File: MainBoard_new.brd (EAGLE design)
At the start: 60 parts, among them T1 BC847, U1 STM32F10XRXT6, Y1 8MHz, Y2 32.768kHz

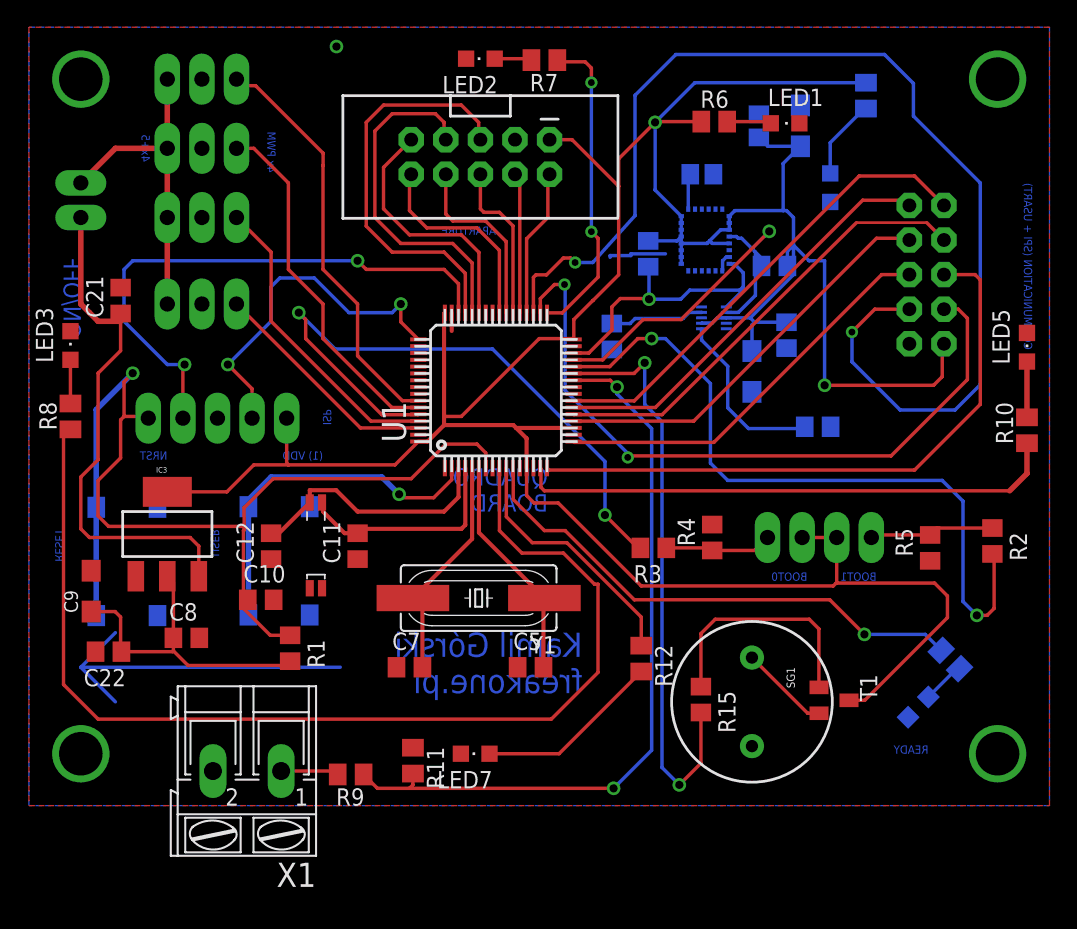
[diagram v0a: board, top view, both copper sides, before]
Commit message: zgubione sygnały przerwań
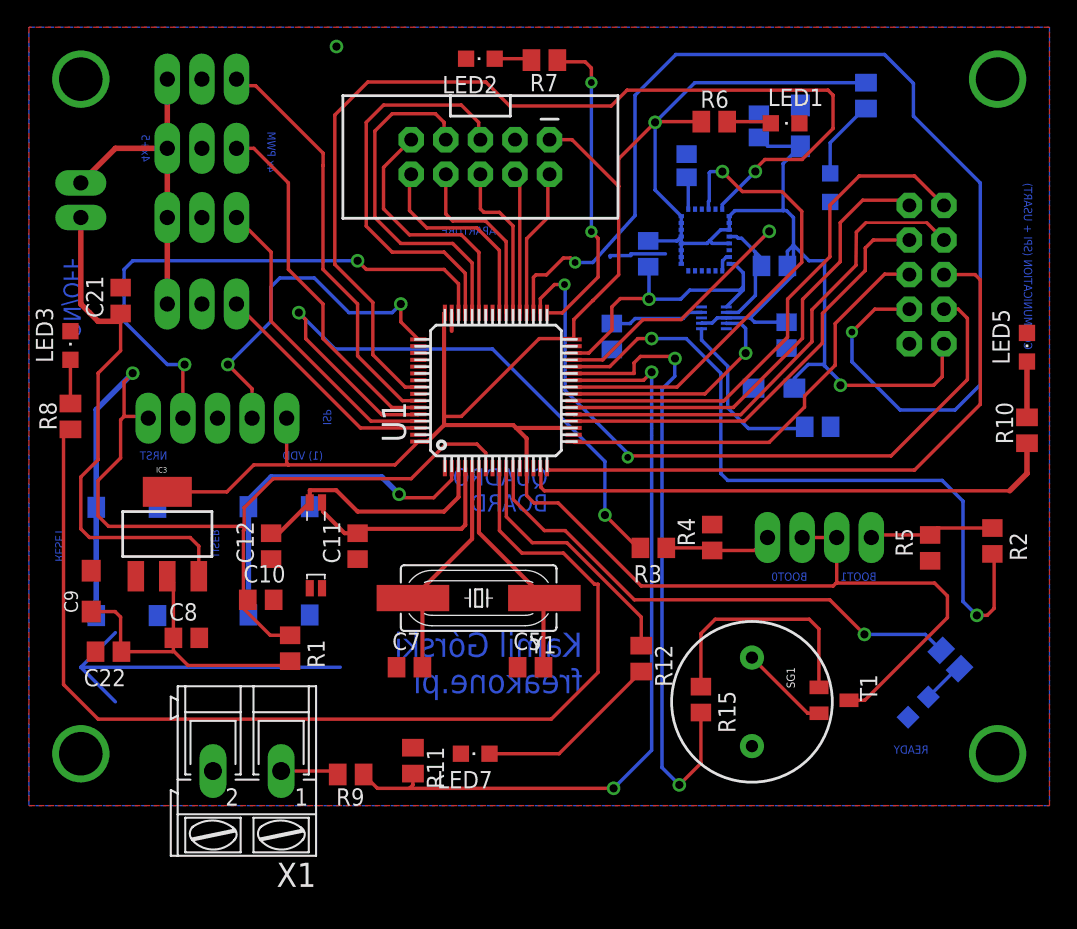
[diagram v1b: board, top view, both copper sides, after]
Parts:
- moved C17 2.03 mm to (44.5, 33.2), turned to 0 degrees
- moved C19 1.28 mm to (38.1, 49.5), turned to 90 degrees
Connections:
- net INT_ACC: now also U1.56
- net INT_GYRO: now also U1.25
- net INT_MAG: now also U1.24
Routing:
- net INT_ACC: track 0.00 -> 75.4 mm, vias 0 -> 1
- net INT_GYRO: track 0.00 -> 35.0 mm, vias 0 -> 1
- net INT_MAG: track 0.00 -> 17.3 mm, vias 0 -> 1
- net MOSI: track 34.9 -> 38.8 mm
- net MISO: track 31.1 -> 34.5 mm
- net BUZZ: track 43.6 -> 46.7 mm
- net SCK: track 33.5 -> 36.4 mm
- net LIPO: track 55.0 -> 57.7 mm
- net RX: track 29.8 -> 32.1 mm
- net SS: track 30.3 -> 32.4 mm
- net BOOT1: track 52.1 -> 53.0 mm
- net 3.3V: track 257.6 -> 258.1 mm

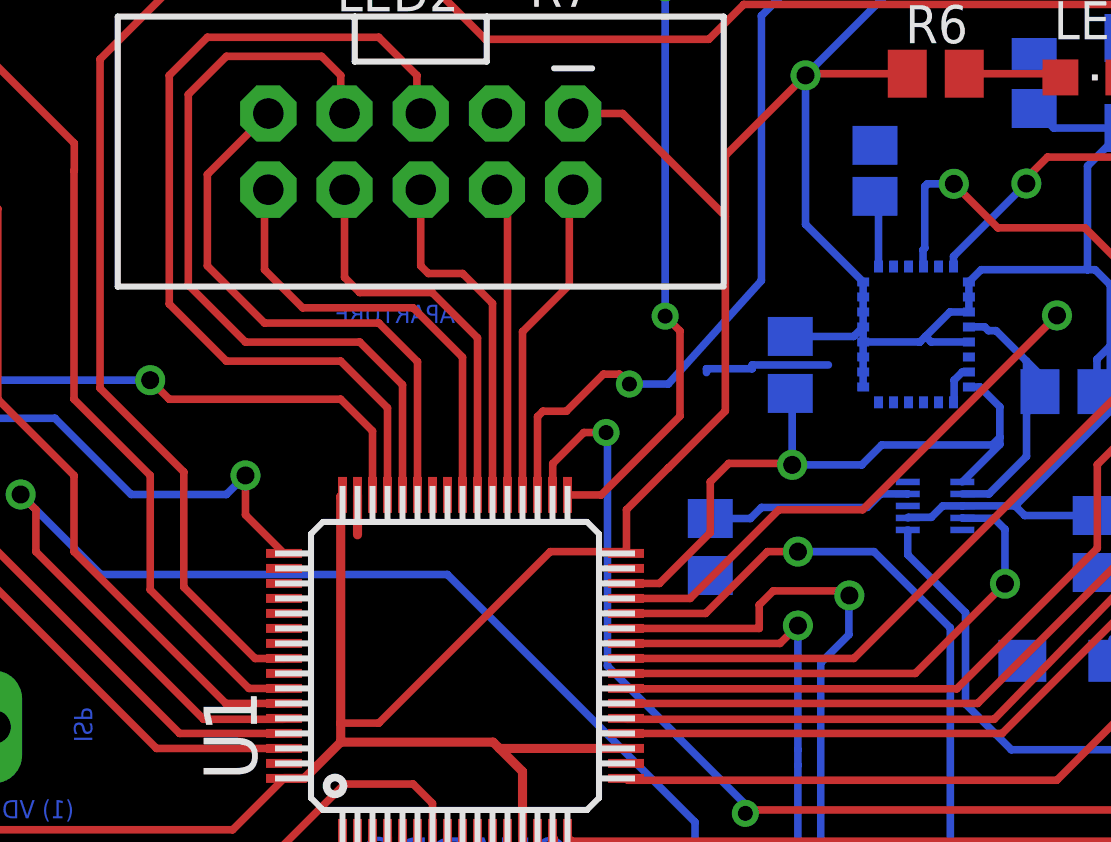
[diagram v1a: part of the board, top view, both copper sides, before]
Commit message: odczyt z czujników
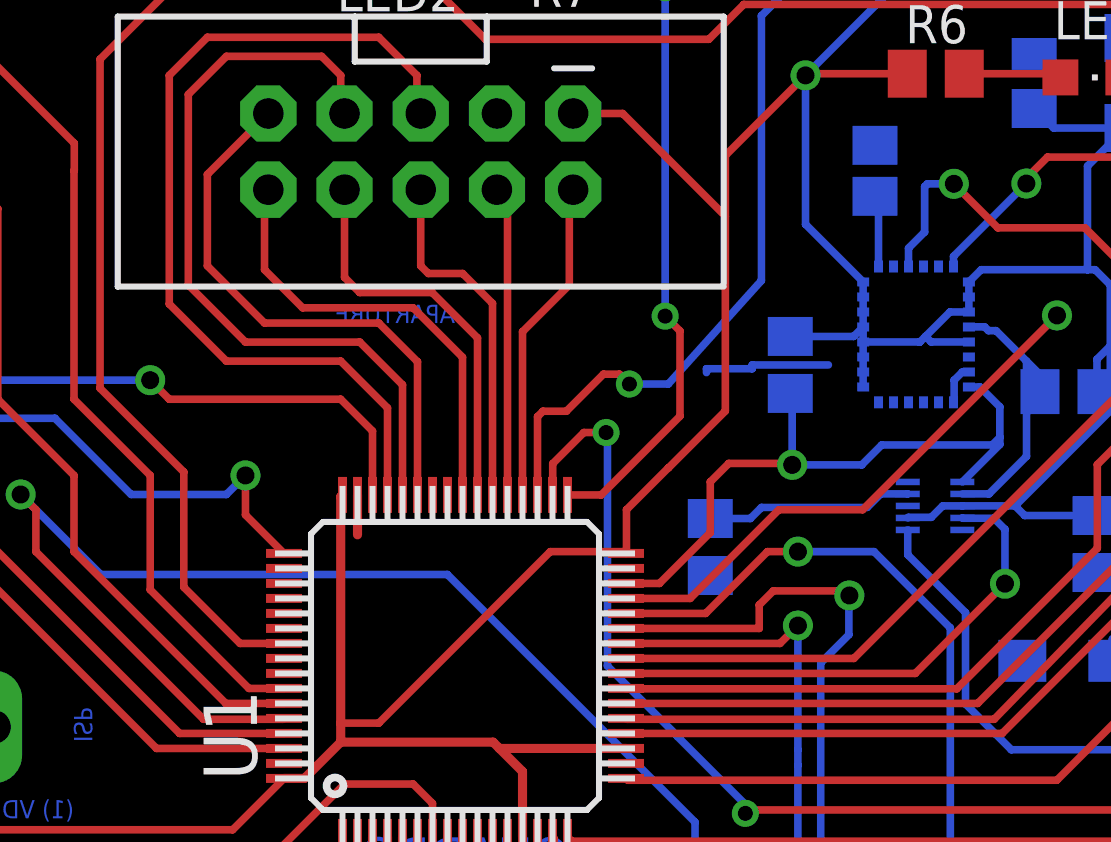
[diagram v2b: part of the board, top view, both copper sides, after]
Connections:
- net INT_ACC: now also U1.55; no longer U1.56
- net INT_GYRO: now also LSM330DLC.P17; no longer LSM330DLC.P18
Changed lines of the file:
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@@
 <grid distance="0" unitdist="inch" unit="inch" style="lines" multiple="1" display="yes" altdistance="0.025" altunitdist="inch" altunit="inch"/>
 <layers>
-<layer number="1" name="Top" color="4" fill="1" visible="yes" active="yes"/>
+<layer number="1" name="Top" color="4" fill="1" visible="no" active="yes"/>
 <layer number="2" name="Route2" color="1" fill="3" visible="no" active="no"/>
 <layer number="3" name="Route3" color="4" fill="3" visible="no" active="no"/>
@@
 <signal name="INT_ACC">
 <contactref element="LSM330DLC" pad="P20"/>
-<contactref element="U1" pad="56"/>
 <wire x1="40.747" y1="46.3315" x2="40.747" y2="46.6731125" width="0.254" layer="16"/>
 <wire x1="40.747" y1="46.6731125" x2="43.17405625" y2="49.10016875" width="0.254" layer="16"/>
@@
 <wire x1="12.298209375" y1="42.27600625" x2="15.089790625" y2="39.484425" width="0.254" layer="1"/>
 <wire x1="15.089790625" y1="39.484425" x2="15.089790625" y2="35.644690625" width="0.254" layer="1"/>
-<wire x1="15.089790625" y1="35.644690625" x2="17.466828125" y2="33.267653125" width="0.254" layer="1"/>
-<wire x1="17.466828125" y1="33.267653125" x2="18.427653125" y2="33.267653125" width="0.254" layer="1"/>
-<wire x1="18.427653125" y1="33.267653125" x2="18.43" y2="33.27" width="0.254" layer="1"/>
+<contactref element="U1" pad="55"/>
+<wire x1="18.43" y1="33.77" x2="16.96448125" y2="33.77" width="0.254" layer="1"/>
+<wire x1="16.96448125" y1="33.77" x2="15.089790625" y2="35.644690625" width="0.254" layer="1"/>
 </signal>
 <signal name="INT_GYRO">
-<contactref element="LSM330DLC" pad="P18"/>
 <contactref element="U1" pad="25"/>
 <wire x1="29.83" y1="33.27" x2="37.42609375" y2="33.27" width="0.254" layer="1"/>
@@
 <via x="40.757209375" y="49.0908375" extent="1-16" drill="0.6" shape="square"/>
 <wire x1="40.757209375" y1="49.0908375" x2="39.876925" y2="49.0908375" width="0.254" layer="16"/>
-<wire x1="39.876925" y1="49.0908375" x2="39.788896875" y2="49.002809375" width="0.254" layer="16"/>
-<wire x1="39.788896875" y1="49.002809375" x2="39.788896875" y2="46.9488" width="0.254" layer="16"/>
-<wire x1="39.788896875" y1="46.9488" x2="39.730209375" y2="46.8901125" width="0.254" layer="16"/>
-<wire x1="39.730209375" y1="46.8901125" x2="39.730209375" y2="46.348290625" width="0.254" layer="16"/>
-<wire x1="39.730209375" y1="46.348290625" x2="39.747" y2="46.3315" width="0.254" layer="16"/>
+<wire x1="39.876925" y1="49.0908375" x2="39.78400625" y2="48.99791875" width="0.254" layer="16"/>
+<contactref element="LSM330DLC" pad="P17"/>
+<wire x1="39.247" y1="46.3315" x2="39.247" y2="46.94625" width="0.254" layer="16"/>
+<wire x1="39.247" y1="46.94625" x2="39.78400625" y2="47.48325625" width="0.254" layer="16"/>
+<wire x1="39.78400625" y1="47.48325625" x2="39.78400625" y2="48.99791875" width="0.254" layer="16"/>
 </signal>
 <signal name="A4">

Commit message: poprawki płytki, kodzik
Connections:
- net 5V: now also JP5.2, JP6.2, JP7.2, JP8.2; no longer JP5.1, JP6.1, JP7.1, JP8.1
- net GND: now also JP5.1, JP6.1, JP7.1, JP8.1; no longer JP5.2, JP6.2, JP7.2, JP8.2
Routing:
- net 5V: track 23.9 -> 29.6 mm
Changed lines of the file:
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@@
 <setting verticaltext="up"/>
 </settings>
-<grid distance="0" unitdist="inch" unit="inch" style="lines" multiple="1" display="yes" altdistance="0.025" altunitdist="inch" altunit="inch"/>
+<grid distance="0.025" unitdist="inch" unit="inch" style="lines" multiple="1" display="yes" altdistance="0.025" altunitdist="inch" altunit="inch"/>
 <layers>
-<layer number="1" name="Top" color="4" fill="1" visible="no" active="yes"/>
+<layer number="1" name="Top" color="4" fill="1" visible="yes" active="yes"/>
 <layer number="2" name="Route2" color="1" fill="3" visible="no" active="no"/>
 <layer number="3" name="Route3" color="4" fill="3" visible="no" active="no"/>
@@
 <contactref element="IC3" pad="1"/>
 <wire x1="20.88" y1="38.72" x2="20.88" y2="37.39" width="0.3048" layer="1"/>
-<contactref element="JP5" pad="2"/>
-<contactref element="JP6" pad="2"/>
-<contactref element="JP7" pad="2"/>
-<contactref element="JP8" pad="2"/>
 <wire x1="41.2595" y1="42.819" x2="41.041" y2="42.819" width="0.254" layer="16"/>
 <wire x1="41.041" y1="42.819" x2="40.767" y2="42.545" width="0.254" layer="16"/>
@@
 <contactref element="SG1" pad="+"/>
 <via x="12.417934375" y="58.27184375" extent="1-16" drill="0.6" shape="square"/>
+<contactref element="JP6" pad="1"/>
+<contactref element="JP7" pad="1"/>
+<contactref element="JP8" pad="1"/>
+<contactref element="JP5" pad="1"/>
 </signal>
 <signal name="SWDIO">
@@
 </signal>
 <signal name="5V">
-<contactref element="JP5" pad="1"/>
-<contactref element="JP6" pad="1"/>
-<contactref element="JP7" pad="1"/>
-<contactref element="JP8" pad="1"/>
 <contactref element="JP9" pad="1"/>
-<wire x1="0" y1="55.88" x2="0" y2="50.8" width="0.4064" layer="1"/>
-<wire x1="0" y1="50.8" x2="0" y2="45.72" width="0.4064" layer="1"/>
-<wire x1="0" y1="45.72" x2="0" y2="39.37" width="0.4064" layer="1"/>
-<wire x1="0" y1="50.8" x2="-3.81" y2="50.8" width="0.4064" layer="1"/>
-<wire x1="-3.81" y1="50.8" x2="-6.35" y2="48.26" width="0.4064" layer="1"/>
+<contactref element="JP5" pad="2"/>
+<contactref element="JP6" pad="2"/>
+<contactref element="JP7" pad="2"/>
+<contactref element="JP8" pad="2"/>
+<wire x1="2.54" y1="39.37" x2="2.54" y2="42.545" width="0.4064" layer="1"/>
+<wire x1="2.54" y1="42.545" x2="2.54" y2="45.72" width="0.4064" layer="1"/>
+<wire x1="2.54" y1="45.72" x2="2.54" y2="50.8" width="0.4064" layer="1"/>
+<wire x1="2.54" y1="50.8" x2="2.54" y2="55.88" width="0.4064" layer="1"/>
+<wire x1="-6.35" y1="48.26" x2="-3.81" y2="48.26" width="0.4064" layer="1"/>
+<wire x1="-3.81" y1="48.26" x2="-2.54" y2="46.99" width="0.4064" layer="1"/>
+<wire x1="-2.54" y1="46.99" x2="-2.54" y2="43.815" width="0.4064" layer="1"/>
+<wire x1="-2.54" y1="43.815" x2="-1.27" y2="42.545" width="0.4064" layer="1"/>
+<wire x1="-1.27" y1="42.545" x2="2.54" y2="42.545" width="0.4064" layer="1"/>
 </signal>
 <signal name="REG1">
